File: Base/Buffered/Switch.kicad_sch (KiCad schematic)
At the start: 25 parts, among them Q1 DMC3071LVT, Q3 LS844

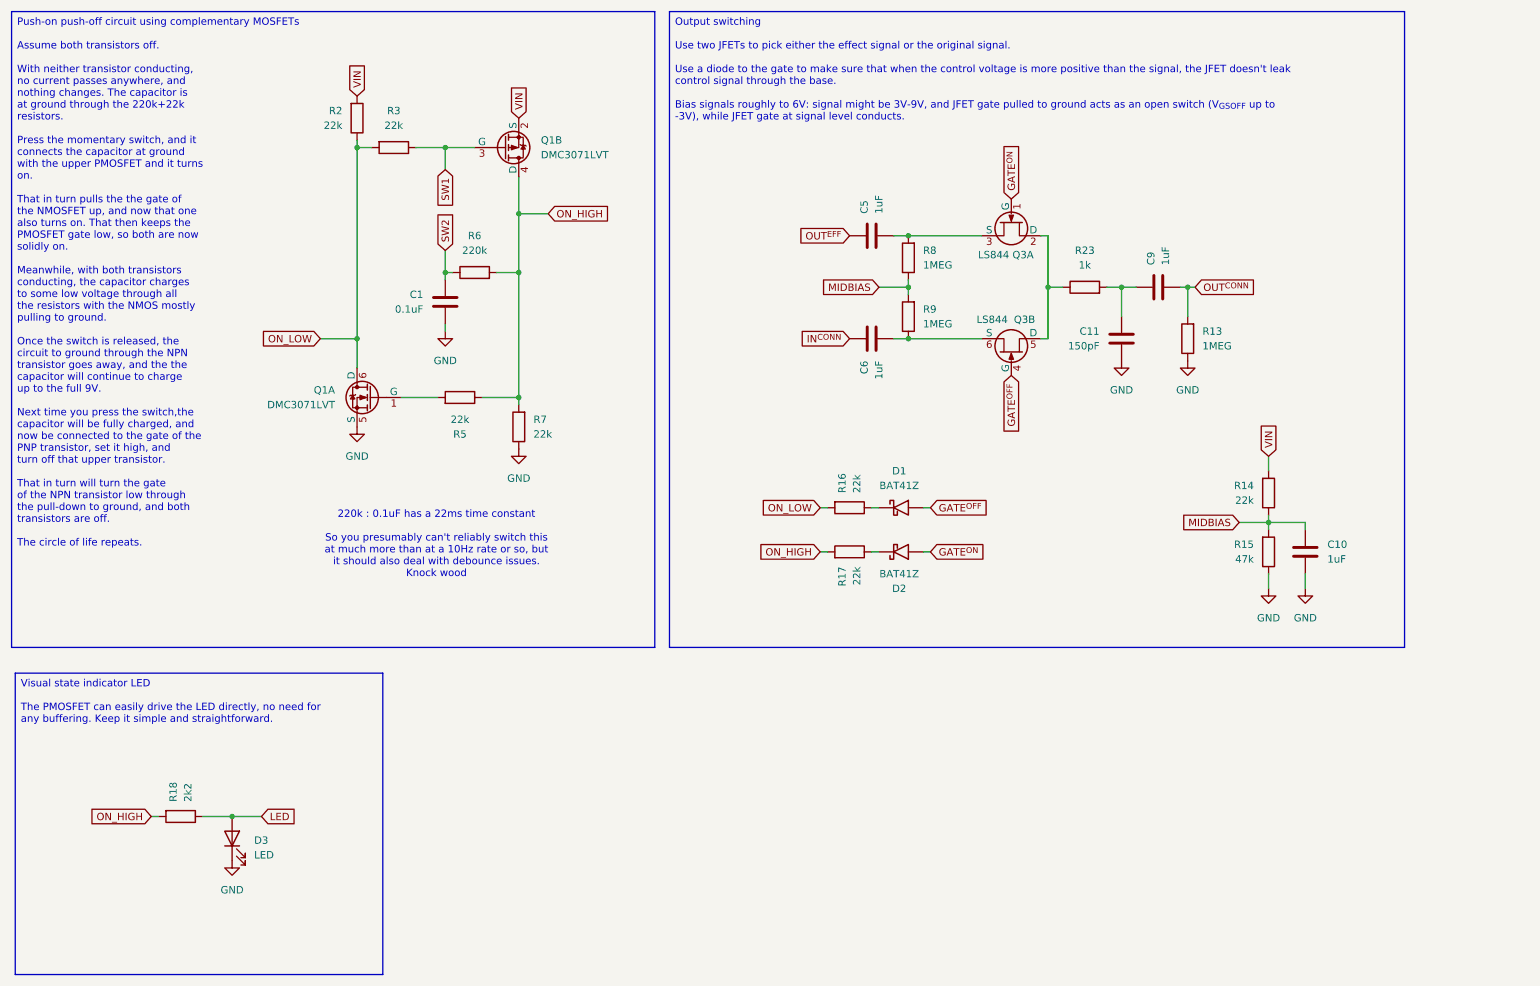
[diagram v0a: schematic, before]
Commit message: Buffered base: use negative rail for JFET switching
This _still_ doesn't do any actual buffering, but with the negative
rail, we now no longer need to rebase the signals to some mid-point
voltage, and we can just leave the signals ground-references and use the
negative rail for switching.

That streamlines the signal path, and will make it easier to just insert
an opamp or two in there too.  But I remain more interested in getting
the switching side sorted out properly, so that's the primary goal here.

This tweaks the push-on push-off circuit a bit too, since taht one now
needs to switch between positive and negative voltages rather than VIN
and ground.

Signed-off-by: Linus Torvalds <torvalds@linux-foundation.org>
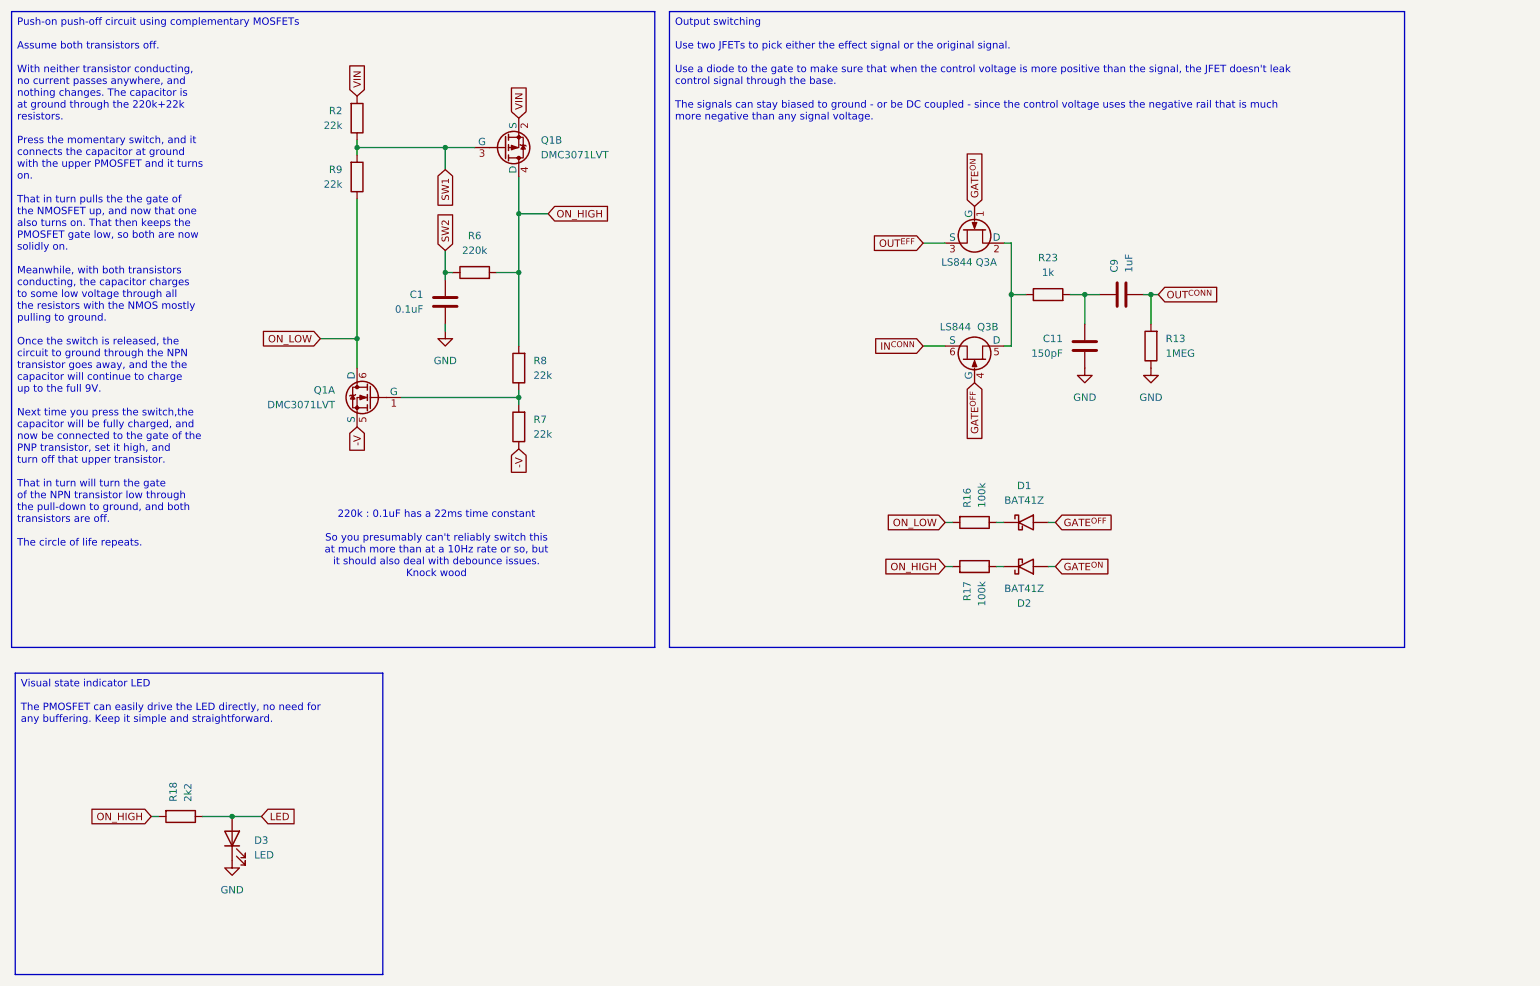
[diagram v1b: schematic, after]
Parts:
- removed C10, C5, C6: 1uF, Capacitor_SMD:C_1206_3216Metric, symbol Device:C
- removed R14, R3, R5: 22k, Resistor_SMD:R_0805_2012Metric, symbol Device:R
- removed R15: 47k, Resistor_SMD:R_0805_2012Metric, symbol Device:R
- R16, R17: value 22k -> 100k
- R8, R9: value 1MEG -> 22k
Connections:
- net GND: no longer Q1.5 (S), R7.1
- net IN^{CONN}: now also Q3.6 (S)
- net ON_HIGH: now also R8.2; no longer R7.2
- net ON_LOW: now also R9.1; no longer R2.1
- net OUT^{EFF}: now also Q3.3 (S)
- net SW1: now also R2.1, R9.2
- net at Q1.1 (G): now also R7.2, R8.1
- removed net MIDBIAS: R8.1, R9.2
- new net -V: Q1.5 (S), R7.1
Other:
- moved on the sheet: C11, C9, D1, D2, Q3A, Q3B, R13, R16, R17, R23

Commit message: Update the buffered base board
The JFET switching worked fine, but since this all started as an
exercise in using MOSFETs, let's just go all in on that, and use the
MOSFETs for switching the signal too.

Due to the body diode, you need two MOSFETs in series for the signal
switching, so it's four MOSFETs instead of two JFETs, but despite that
the end result is actually simpler.  And those dual MOSFET things are
common and dirt cheap, unlike the special matched JFET package.

Since I can just continue to use the dual complementary MOSFETs, I can
use PMOS for one signal and NMOS for the other, and share all the gate
circuit.  Plus no need for a diode to protect the gate current messing
with the signal.

Also update the resistor value in the switching circuit and make the
time constant be 100ms.  That seems to make it more reliable in testing,
although I'm not convinced my testing with the original value was all
that great.  The soft-switch circuit does seem to work, though.

Also, since the LED pin on the board connectors has never been used,
let's just re-purpose that as a negative voltage pin for the effect
board.  If some effect board wants to touch the LED status, it might as
well just connect to the LED itself.  Having access to a dual voltage
rail would seem to be a lot more important.

Finally - and probably most importantly for actual sound and current
effects boards - add a low-pass filter on the voltage lines.  Because as
expected, the negative power supply did add a lot of noise to the VIN
line.

The base board itself doesn't actually care, but the effects boards do.

An actual LDO would be better, but I don't have any simple fixed ones in
my parts library (except for the 5V one, which seems a bit sad).
Current effects boards don't use a lot of current and only care about
the voltage being stable, so let's try this simple model.

Signed-off-by: Linus Torvalds <torvalds@linux-foundation.org>
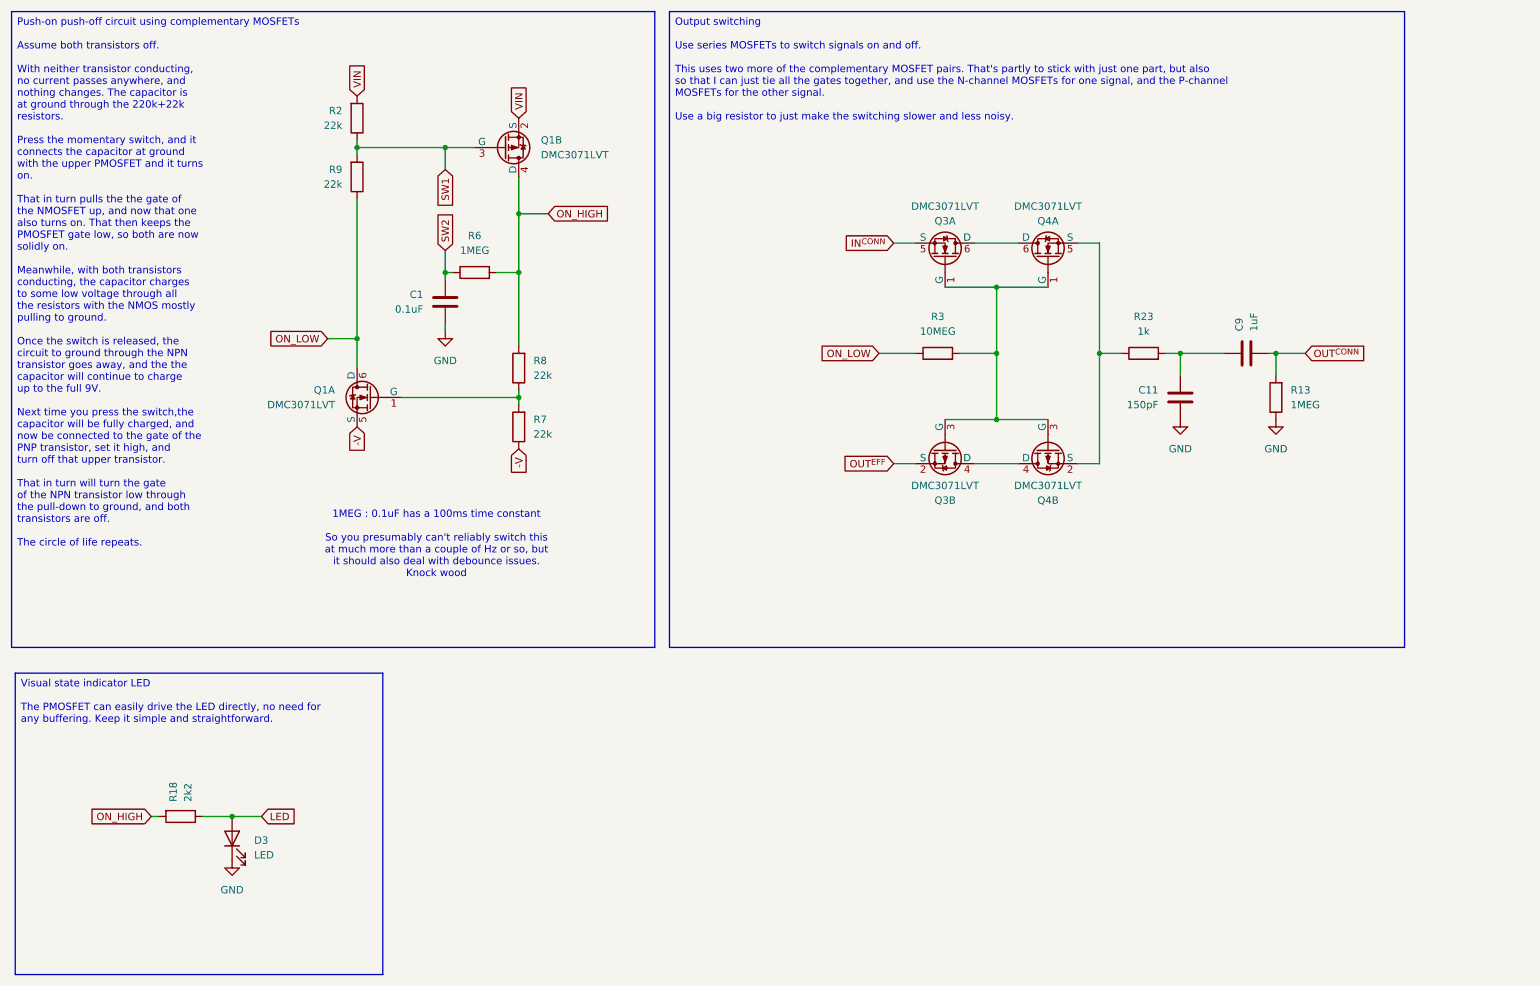
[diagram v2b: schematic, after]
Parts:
- removed D1, D2: BAT41Z, Diode_SMD:D_SOD-123, symbol Mylib:BAT41ZFILM
- removed Q3: LS844, Package_TO_SOT_SMD:SOT-23-6, symbol Mylib:LS844
- removed R16, R17: 100k, Resistor_SMD:R_0805_2012Metric, symbol Device:R
- added Q3, Q4: DMC3071LVT, Package_TO_SOT_SMD:TSOT-23-6, symbol Mylib:DMC3071LVT
- added R3: 10MEG, Resistor_SMD:R_0805_2012Metric, symbol Device:R
- R6: value 220k -> 1MEG
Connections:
- net IN^{CONN}: now also Q3.5 (S)
- net ON_LOW: now also R3.1
- net OUT^{EFF}: now also Q3.2 (S)
- net at R23.1: now also Q4.2 (S), Q4.5 (S)
- new net: Q3.1 (G), Q3.3 (G), Q4.1 (G), Q4.3 (G), R3.2
- new net: Q3.4 (D), Q4.4 (D)
- new net: Q3.6 (D), Q4.6 (D)
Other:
- note added: "1MEG : 0.1uF has a 100ms time constant So you presumably can't reliably switch this at much more than a couple of Hz or so, but it should also deal with debounce issues. Knock wood"
- note removed: "220k : 0.1uF has a 22ms time constant So you presumably can't reliably switch this at much more than at a 10Hz rate or so, but it should also deal with debounce issues. Knock wood"
- moved on the sheet: C11, C9, R13, R23

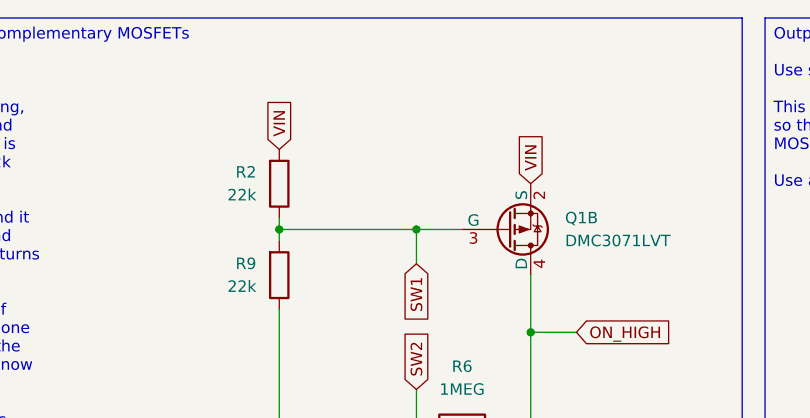
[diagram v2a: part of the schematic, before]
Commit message: Try LDO for positive voltage rail cleaning
As mentioned, I don't think I'll actually build this, because it seems
pointlessly complicated.  But I did the basic design and layout for it
just in case.

I think I'll go back to the single-rail design and keep the MOSFET
switching.

I also think I need to come up with a new project.  I'm kind of running
out of ideas of small projects to do that I can build and test.  I like
the switching circuit, but I'm losing interest in the effects board side
since I still can't actually play guitar.

Signed-off-by: Linus Torvalds <torvalds@linux-foundation.org>
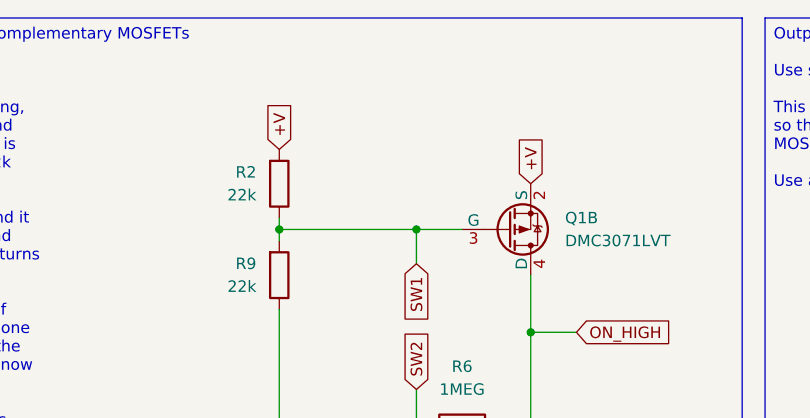
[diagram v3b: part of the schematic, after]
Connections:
- net VIN renamed +V
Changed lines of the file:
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@@
 		)
 	)
-	(global_label "VIN"
+	(global_label "+V"
 		(shape input)
 		(at 102.87 33.02 90)
@@
 		)
 		(property "Intersheetrefs" "${INTERSHEET_REFS}"
-			(at 102.87 27.0109 90)
+			(at 102.87 27.3738 90)
 			(hide yes)
 			(effects
@@
 		)
 	)
-	(global_label "VIN"
+	(global_label "+V"
 		(shape input)
 		(at 74.93 29.21 90)
@@
 		)
 		(property "Intersheetrefs" "${INTERSHEET_REFS}"
-			(at 74.93 23.2009 90)
+			(at 74.93 23.5638 90)
 			(hide yes)
 			(effects
